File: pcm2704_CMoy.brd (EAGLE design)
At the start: 100.3 x 77.5 mm, 87 parts, among them IC3 7815DT, IC4 tsr 1-2433, IC5 7915TV, Q1 12MHz, U1 PCM2704, U2 OPA2134P, U3 TC962EPA, X2 PN61729-S, X5 22-23-2031, X6 22-23-2031

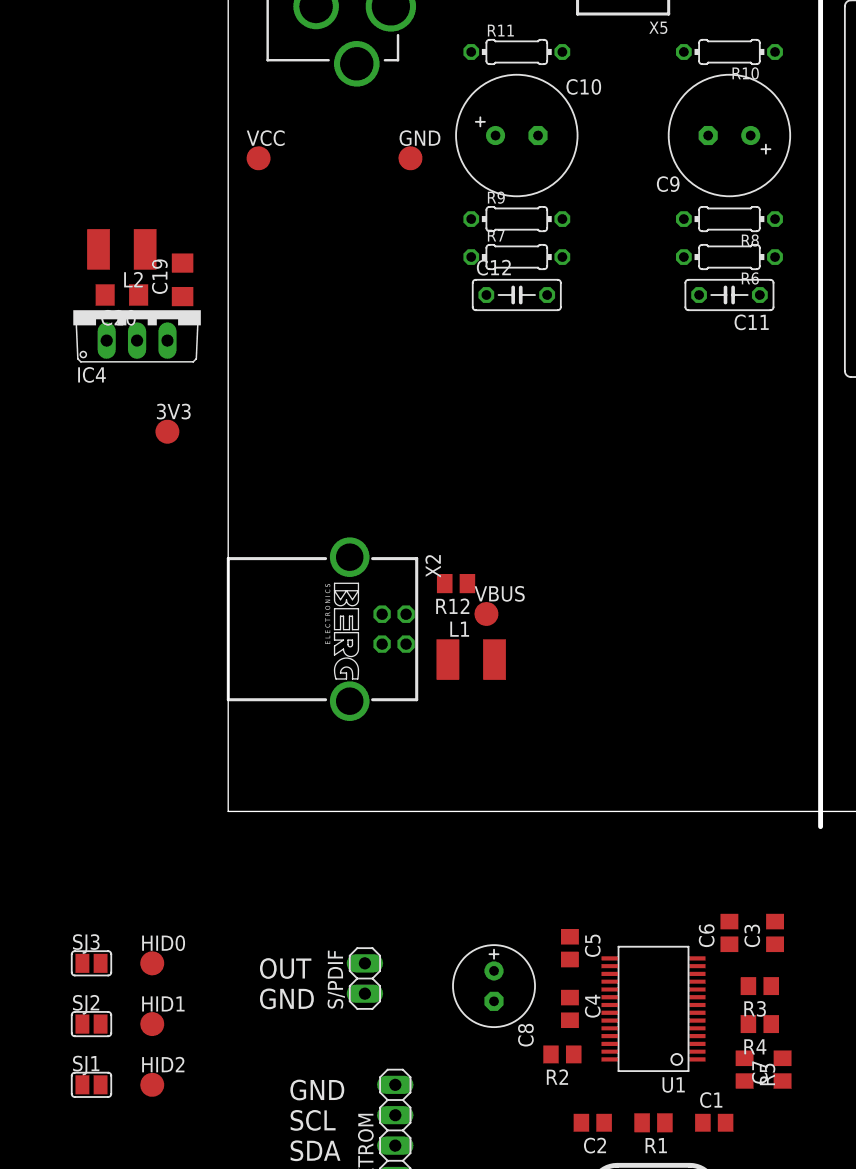
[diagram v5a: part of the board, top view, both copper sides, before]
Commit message: - Modified capacitor names to match the datasheet example (DAC)
 - Fixed a few capacitor values that did not match the datasheet example (DAC)
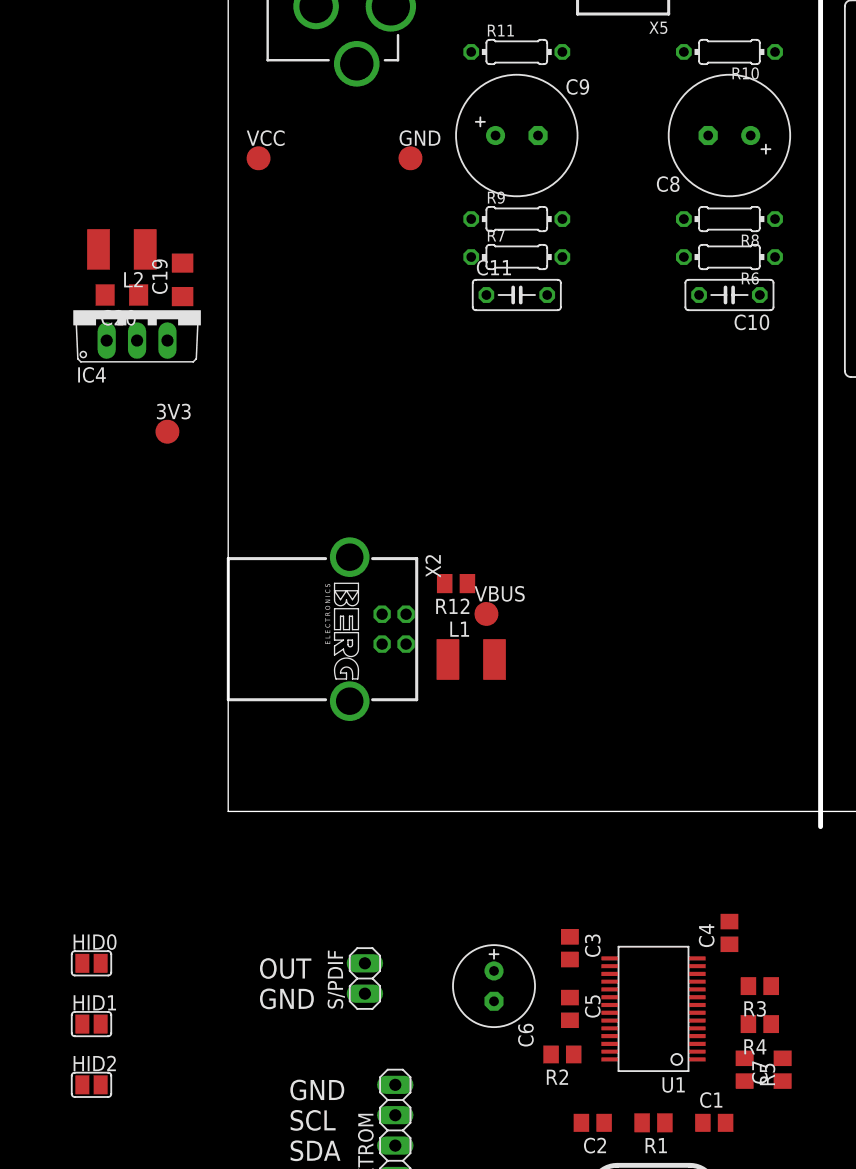
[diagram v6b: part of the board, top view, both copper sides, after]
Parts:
- removed C12: 22nF, rcl:C050-025X075
- removed SJ1, SJ2, SJ3: (no value), jumper:SJ
- C10: value 100uF -> 22nF; device rcl:E3,5-10 -> rcl:C050-025X075
- C5: value 1uF -> 10uF
- C6: value 1uF -> 10uF; device rcl:C0805 -> rcl:E2,5-7
- C7: value 1uF -> 0.1uF
- C8: value 10uF -> 100uF; device rcl:E2,5-7 -> rcl:E3,5-10
- HID0, HID1, HID2: value TPTP20R -> (none); device testpad:TP20R -> jumper:SJ
- moved C8 73.8 mm to (41.9, 56.5), turned to 180 degrees
- moved C10 22.2 mm to (41.9, 43.2), turned to 180 degrees
- moved C6 20.2 mm to (22.2, -14.6), turned to 270 degrees
- moved C11 17.8 mm to (24.1, 43.2), turned to 0 degrees
- moved C9 17.8 mm to (24.1, 56.5), turned to 0 degrees
- moved C3 17.2 mm to (28.6, -11.4), turned to 270 degrees
- moved C4 14.8 mm to (41.9, -10.2), turned to 90 degrees
- moved C5 5.08 mm to (28.6, -16.5)
- moved HID0 5.08 mm to (-11.4, -12.7)
- moved HID1 5.08 mm to (-11.4, -17.8)
- moved HID2 5.08 mm to (-11.4, -22.9)
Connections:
- removed net N$2: R12.2, X2.1
- net +3V3: now also C3.1, C5.2; no longer C5.1, C6.2
- net DAC_OUT_LEFT: now also C9.-; no longer C10.-
- net DAC_OUT_RIGHT: now also C8.-; no longer C9.-
- net GND: now also C3.2, C5.1, C6.-, HID0.2, HID1.2, HID2.2, R12.1; no longer C5.2, C6.1, C8.-, SJ1.2, SJ2.2, SJ3.2
- net N$12: now also HID2.1; no longer HID2.TP, SJ1.1
- net N$15: now also HID1.1; no longer HID1.TP, SJ2.1
- net N$16: now also HID0.1; no longer HID0.TP, SJ3.1
- net N$26: now also C10.2; no longer C11.2
- net N$27: now also C11.2; no longer C12.2
- net N$28: now also C10.1, C8.+; no longer C11.1, C9.+
- net N$29: now also C11.1, C9.+; no longer C10.+, C12.1
- net VBUS: now also R12.2, X2.1; no longer R12.1
- net VCOM: now also C6.+; no longer C8.+
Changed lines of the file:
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@@
 <element name="C1" library="rcl" package="C0805" value="22pF" x="40.64" y="-26.035"/>
 <element name="C2" library="rcl" package="C0805" value="22pF" x="30.48" y="-26.035" rot="R180"/>
-<element name="C3" library="rcl" package="C0805" value="1uF" x="45.72" y="-10.16" rot="R90"/>
-<element name="C4" library="rcl" package="C0805" value="1uF" x="28.575" y="-16.51" rot="R270"/>
-<element name="C5" library="rcl" package="C0805" value="1uF" x="28.575" y="-11.43" rot="R270"/>
-<element name="C6" library="rcl" package="C0805" value="1uF" x="41.91" y="-10.16" rot="R90"/>
-<element name="C7" library="rcl" package="C0805" value="1uF" x="46.355" y="-21.59" rot="R90"/>
-<element name="C8" library="rcl" package="E2,5-7" value="10uF" x="22.225" y="-14.605" rot="R270"/>
-<element name="C9" library="rcl" package="E3,5-10" value="100uF" x="41.91" y="56.515" rot="R180"/>
-<element name="C10" library="rcl" package="E3,5-10" value="100uF" x="24.13" y="56.515"/>
-<element name="C11" library="rcl" package="C050-025X075" value="22nF" x="41.91" y="43.18" rot="R180"/>
-<element name="C12" library="rcl" package="C050-025X075" value="22nF" x="24.13" y="43.18"/>
+<element name="C5" library="rcl" package="C0805" value="10uF" x="28.575" y="-16.51" rot="R270"/>
+<element name="C3" library="rcl" package="C0805" value="1uF" x="28.575" y="-11.43" rot="R270"/>
+<element name="C4" library="rcl" package="C0805" value="1uF" x="41.91" y="-10.16" rot="R90"/>
+<element name="C7" library="rcl" package="C0805" value="0.1uF" x="46.355" y="-21.59" rot="R90"/>
+<element name="C6" library="rcl" package="E2,5-7" value="10uF" x="22.225" y="-14.605" rot="R270"/>
+<element name="C8" library="rcl" package="E3,5-10" value="100uF" x="41.91" y="56.515" rot="R180"/>
+<element name="C9" library="rcl" package="E3,5-10" value="100uF" x="24.13" y="56.515"/>
+<element name="C10" library="rcl" package="C050-025X075" value="22nF" x="41.91" y="43.18" rot="R180"/>
+<element name="C11" library="rcl" package="C050-025X075" value="22nF" x="24.13" y="43.18"/>
 <element name="Q1" library="crystal" package="HC49/S" value="12MHz" x="35.56" y="-31.75" rot="R180"/>
 <element name="R5" library="rcl" package="R0805" value="1k5" x="43.18" y="-21.59" rot="R270"/>
@@
 <element name="S/PDIF" library="pinhead" package="1X02" value="" x="11.43" y="-13.97" rot="R90"/>
 <element name="EXTROM" library="pinhead" package="1X04" value="" x="13.97" y="-26.67" rot="R90"/>
-<element name="HID2" library="testpad" package="TP20R" value="TPTP20R" x="-6.35" y="-22.86"/>
-<element name="HID1" library="testpad" package="TP20R" value="TPTP20R" x="-6.35" y="-17.78"/>
-<element name="HID0" library="testpad" package="TP20R" value="TPTP20R" x="-6.35" y="-12.7"/>
-<element name="SJ1" library="jumper" package="SJ" value="" x="-11.43" y="-22.86"/>
-<element name="SJ2" library="jumper" package="SJ" value="" x="-11.43" y="-17.78"/>
-<element name="SJ3" library="jumper" package="SJ" value="" x="-11.43" y="-12.7"/>
+<element name="HID2" library="jumper" package="SJ" value="" x="-11.43" y="-22.86"/>
+<element name="HID1" library="jumper" package="SJ" value="" x="-11.43" y="-17.78"/>
+<element name="HID0" library="jumper" package="SJ" value="" x="-11.43" y="-12.7"/>
 <element name="3V3" library="testpad" package="TP20R" value="TPTP20R" x="-5.08" y="31.75"/>
 <element name="VBUS" library="testpad" package="TP20R" value="TPTP20R" x="21.59" y="16.51"/>
@@
 <signal name="VBUS">
 <contactref element="U1" pad="21"/>
-<contactref element="R12" pad="1"/>
 <contactref element="VBUS" pad="TP"/>
 <contactref element="R13" pad="1"/>
+<contactref element="X2" pad="1"/>
+<contactref element="R12" pad="2"/>
 <wire x1="31.904" y1="-16.185" x2="-26.35" y2="-31.75" width="0" layer="19" extent="1-1"/>
 <wire x1="21.59" y1="16.51" x2="31.904" y2="-16.185" width="0" layer="19" extent="1-1"/>
-<wire x1="20" y1="19.05" x2="21.59" y2="16.51" width="0" layer="19" extent="1-1"/>
+<wire x1="18.1" y1="19.05" x2="21.59" y2="16.51" width="0" layer="19" extent="1-1"/>
+<wire x1="14.87" y1="13.99" x2="18.1" y2="19.05" width="0" layer="19" extent="1-1"/>
 </signal>
 <signal name="GND">
@@
 <contactref element="C2" pad="2"/>
 <contactref element="U1" pad="19"/>
-<contactref element="C8" pad="-"/>
+<contactref element="C6" pad="-"/>
 <contactref element="U1" pad="17"/>
-<contactref element="C5" pad="2"/>
+<contactref element="C3" pad="2"/>
 <contactref element="R6" pad="1"/>
 <contactref element="R7" pad="1"/>
@@
 <contactref element="IC4" pad="2"/>
 <contactref element="LED1" pad="K"/>
-<contactref element="SJ1" pad="2"/>
-<contactref element="SJ2" pad="2"/>
-<contactref element="SJ3" pad="2"/>
 <contactref element="CN1" pad="GND"/>
 <contactref element="GND" pad="TP"/>
@@
 <contactref element="U1" pad="11"/>
 <contactref element="U1" pad="12"/>
-<contactref element="C6" pad="1"/>
 <contactref element="C4" pad="1"/>
+<contactref element="C5" pad="1"/>
+<contactref element="HID2" pad="2"/>
+<contactref element="HID1" pad="2"/>
+<contactref element="HID0" pad="2"/>
+<contactref element="R12" pad="1"/>
 <wire x1="90.17" y1="64.77" x2="86.36" y2="71.12" width="0" layer="19" extent="1-1"/>
 <wire x1="92.71" y1="64.77" x2="90.17" y2="64.77" width="0" layer="19" extent="1-1"/>
@@
 <wire x1="12.87" y1="13.99" x2="10.16" y2="21.26" width="0" layer="19" extent="1-1"/>
 <wire x1="10.16" y1="9.22" x2="12.87" y2="13.99" width="0" layer="19" extent="1-1"/>
+<wire x1="20" y1="19.05" x2="12.87" y2="13.99" width="0" layer="19" extent="1-1"/>
 <wire x1="11.43" y1="-12.7" x2="10.16" y2="9.22" width="0" layer="19" extent="1-1"/>
 <wire x1="13.97" y1="-22.86" x2="11.43" y2="-12.7" width="0" layer="19" extent="1-1"/>
@@
 <signal name="VCOM">
 <contactref element="U1" pad="18"/>
-<contactref element="C8" pad="+"/>
+<contactref element="C6" pad="+"/>
 <wire x1="22.225" y1="-13.335" x2="31.904" y2="-14.235" width="0" layer="19" extent="1-1"/>
 </signal>
@@
 <signal name="N$26">
 <contactref element="R6" pad="2"/>
-<contactref element="C11" pad="2"/>
+<contactref element="C10" pad="2"/>
 <wire x1="39.37" y1="43.18" x2="38.1" y2="46.355" width="0" layer="19" extent="1-1"/>
 </signal>
 <signal name="N$27">
 <contactref element="R7" pad="2"/>
-<contactref element="C12" pad="2"/>
+<contactref element="C11" pad="2"/>
 <wire x1="26.67" y1="43.18" x2="27.94" y2="46.355" width="0" layer="19" extent="1-1"/>
 </signal>
 <signal name="N$28">
-<contactref element="C9" pad="+"/>
-<contactref element="C11" pad="1"/>
+<contactref element="C8" pad="+"/>
+<contactref element="C10" pad="1"/>
 <contactref element="R8" pad="2"/>
 <contactref element="U1" pad="15"/>
@@
 <signal name="DAC_OUT_RIGHT">
 <contactref element="R10" pad="2"/>
-<contactref element="C9" pad="-"/>
+<contactref element="C8" pad="-"/>
 <contactref element="X5" pad="3"/>
 <contactref element="X6" pad="3"/>
@@
 </signal>
 <signal name="DAC_OUT_LEFT">
-<contactref element="C10" pad="-"/>
+<contactref element="C9" pad="-"/>
 <contactref element="R11" pad="2"/>
 <contactref element="X5" pad="1"/>
@@
 <signal name="N$29">
 <contactref element="U1" pad="14"/>
-<contactref element="C10" pad="+"/>
-<contactref element="C12" pad="1"/>
+<contactref element="C9" pad="+"/>
+<contactref element="C11" pad="1"/>
 <contactref element="R9" pad="2"/>
 <wire x1="27.94" y1="49.53" x2="22.352" y2="56.515" width="0" layer="19" extent="1-1"/>
@@
 <signal name="N$12">
 <contactref element="U1" pad="24"/>
-<contactref element="HID2" pad="TP"/>
-<contactref element="SJ1" pad="1"/>
-<wire x1="-6.35" y1="-22.86" x2="-12.192" y2="-22.86" width="0" layer="19" extent="1-1"/>
-<wire x1="31.904" y1="-18.135" x2="-6.35" y2="-22.86" width="0" layer="19" extent="1-1"/>
+<contactref element="HID2" pad="1"/>
+<wire x1="31.904" y1="-18.135" x2="-12.192" y2="-22.86" width="0" layer="19" extent="1-1"/>
 </signal>
 <signal name="N$15">
 <contactref element="U1" pad="23"/>
-<contactref element="HID1" pad="TP"/>
-<contactref element="SJ2" pad="1"/>
-<wire x1="-6.35" y1="-17.78" x2="-12.192" y2="-17.78" width="0" layer="19" extent="1-1"/>
-<wire x1="31.904" y1="-17.485" x2="-6.35" y2="-17.78" width="0" layer="19" extent="1-1"/>
+<contactref element="HID1" pad="1"/>
+<wire x1="31.904" y1="-17.485" x2="-12.192" y2="-17.78" width="0" layer="19" extent="1-1"/>
 </signal>
 <signal name="N$16">
 <contactref element="U1" pad="22"/>
-<contactref element="HID0" pad="TP"/>
-<contactref element="SJ3" pad="1"/>
-<wire x1="-6.35" y1="-12.7" x2="-12.192" y2="-12.7" width="0" layer="19" extent="1-1"/>
-<wire x1="31.904" y1="-16.835" x2="-6.35" y2="-12.7" width="0" layer="19" extent="1-1"/>
+<contactref element="HID0" pad="1"/>
+<wire x1="31.904" y1="-16.835" x2="-12.192" y2="-12.7" width="0" layer="19" extent="1-1"/>
 </signal>
 <signal name="+12V">
@@
 <contactref element="U1" pad="10"/>
 <contactref element="U1" pad="13"/>
-<contactref element="C6" pad="2"/>
+<contactref element="C4" pad="2"/>
 <contactref element="U1" pad="16"/>
-<contactref element="C5" pad="1"/>
+<contactref element="C3" pad="1"/>
 <contactref element="U1" pad="20"/>
-<contactref element="C4" pad="2"/>
+<contactref element="C5" pad="2"/>
 <contactref element="EXTROM" pad="1"/>
 <contactref element="Q2" pad="3"/>
@@
 <wire x1="72.39" y1="-7.62" x2="91.44" y2="-21.59" width="0" layer="19" extent="1-1"/>
 </signal>
-<signal name="N$2">
-<contactref element="X2" pad="1"/>
-<contactref element="R12" pad="2"/>
-<wire x1="14.87" y1="13.99" x2="18.1" y2="19.05" width="0" layer="19" extent="1-1"/>
-</signal>
 <signal name="N$38">

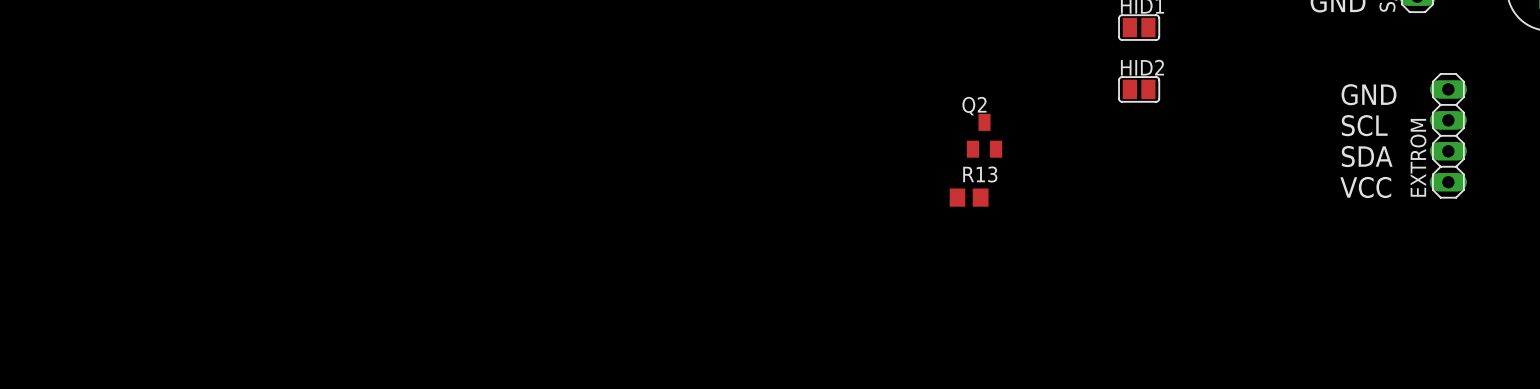
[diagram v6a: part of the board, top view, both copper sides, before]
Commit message: - Removed the external rom connector, because it does not support descriptor overwriting in self powered mode
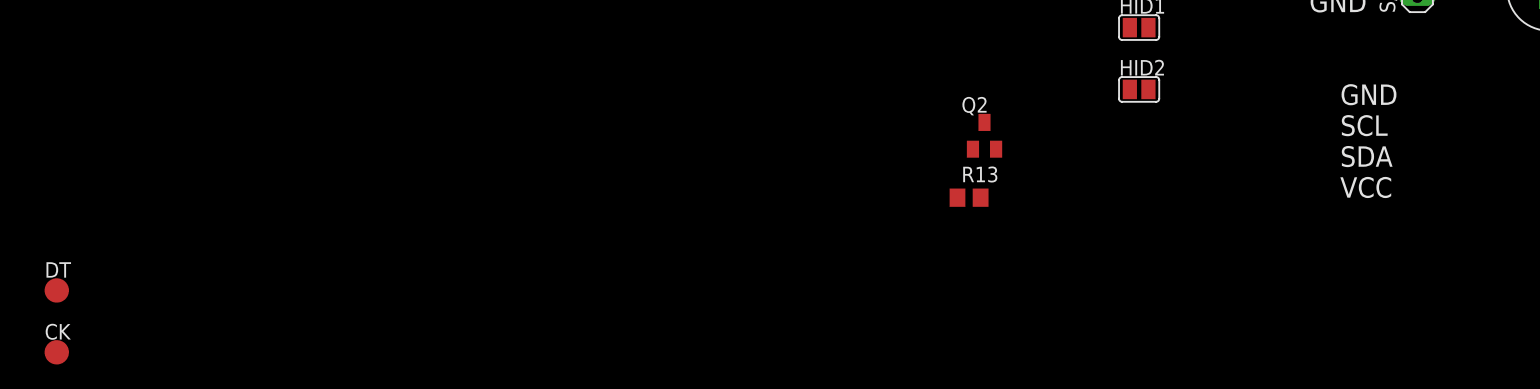
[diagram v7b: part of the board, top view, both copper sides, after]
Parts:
- removed EXTROM: (no value), pinhead:1X04
- added CK, DT: TPTP20R, testpad:TP20R
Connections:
- net +3V3: no longer EXTROM.1
- net GND: no longer EXTROM.4
- net N$20: now also DT.TP; no longer EXTROM.2
- net N$9: now also CK.TP; no longer EXTROM.3
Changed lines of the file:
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@@
 <element name="R21" library="rcl" package="0204/7" value="470R" x="59.69" y="72.39"/>
 <element name="S/PDIF" library="pinhead" package="1X02" value="" x="11.43" y="-13.97" rot="R90"/>
-<element name="EXTROM" library="pinhead" package="1X04" value="" x="13.97" y="-26.67" rot="R90"/>
 <element name="HID2" library="jumper" package="SJ" value="" x="-11.43" y="-22.86"/>
 <element name="HID1" library="jumper" package="SJ" value="" x="-11.43" y="-17.78"/>
@@
 <element name="Q2" library="semicon-smd-ipc" package="SOT23" value="" x="-24.13" y="-26.67"/>
 <element name="R13" library="rcl" package="R0805" value="10K" x="-25.4" y="-31.75"/>
+<element name="DT" library="testpad" package="TP20R" value="TPTP20R" x="-100.33" y="-39.37"/>
+<element name="CK" library="testpad" package="TP20R" value="TPTP20R" x="-100.33" y="-44.45"/>
 </elements>
 <signals>
@@
 <contactref element="X6" pad="2"/>
 <contactref element="S/PDIF" pad="2"/>
-<contactref element="EXTROM" pad="4"/>
 <contactref element="C19" pad="1"/>
 <contactref element="C20" pad="1"/>
@@
 <wire x1="20" y1="19.05" x2="12.87" y2="13.99" width="0" layer="19" extent="1-1"/>
 <wire x1="11.43" y1="-12.7" x2="10.16" y2="9.22" width="0" layer="19" extent="1-1"/>
-<wire x1="13.97" y1="-22.86" x2="11.43" y2="-12.7" width="0" layer="19" extent="1-1"/>
-<wire x1="22.225" y1="-15.875" x2="13.97" y2="-22.86" width="0" layer="19" extent="1-1"/>
+<wire x1="22.225" y1="-15.875" x2="11.43" y2="-12.7" width="0" layer="19" extent="1-1"/>
 <wire x1="28.575" y1="-15.56" x2="22.225" y2="-15.875" width="0" layer="19" extent="1-1"/>
 <wire x1="28.575" y1="-12.38" x2="28.575" y2="-15.56" width="0" layer="19" extent="1-1"/>
@@
 </signal>
 <signal name="N$20">
-<contactref element="EXTROM" pad="2"/>
 <contactref element="R5" pad="2"/>
 <contactref element="U1" pad="3"/>
-<wire x1="39.216" y1="-19.435" x2="43.18" y2="-22.54" width="0" layer="19" extent="1-1"/>
-<wire x1="13.97" y1="-27.94" x2="39.216" y2="-19.435" width="0" layer="19" extent="1-1"/>
+<contactref element="DT" pad="TP"/>
+<wire x1="39.216" y1="-19.435" x2="-100.33" y2="-39.37" width="0" layer="19" extent="1-1"/>
+<wire x1="43.18" y1="-22.54" x2="39.216" y2="-19.435" width="0" layer="19" extent="1-1"/>
 </signal>
 <signal name="N$26">
@@
 <signal name="N$9">
 <contactref element="U1" pad="2"/>
-<contactref element="EXTROM" pad="3"/>
-<wire x1="13.97" y1="-25.4" x2="39.216" y2="-20.085" width="0" layer="19" extent="1-1"/>
+<contactref element="CK" pad="TP"/>
+<wire x1="39.216" y1="-20.085" x2="-100.33" y2="-44.45" width="0" layer="19" extent="1-1"/>
 </signal>
 <signal name="N$12">
@@
 <contactref element="U1" pad="20"/>
 <contactref element="C5" pad="2"/>
-<contactref element="EXTROM" pad="1"/>
 <contactref element="Q2" pad="3"/>
-<wire x1="13.97" y1="-30.48" x2="-24.13" y2="-25.57" width="0" layer="19" extent="1-1"/>
-<wire x1="28.575" y1="-17.46" x2="13.97" y2="-30.48" width="0" layer="19" extent="1-1"/>
+<wire x1="28.575" y1="-17.46" x2="-24.13" y2="-25.57" width="0" layer="19" extent="1-1"/>
 <wire x1="31.904" y1="-18.785" x2="28.575" y2="-17.46" width="0" layer="19" extent="1-1"/>
 <wire x1="31.904" y1="-19.435" x2="31.904" y2="-18.785" width="0" layer="19" extent="1-1"/>
